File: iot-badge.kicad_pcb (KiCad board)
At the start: 2 copper layers, 70 x 100 mm, 30 parts, among them J1 USB_C_Receptacle_USB2.0, Q1 BC847, Q2 BC847, SW1 SW_Push, SW2 SW_Push, SW3 SW_Push, SW4 SW_Push, SW5 SW_Push, SW6 SW_Push, U1 ESP32-WROOM-32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

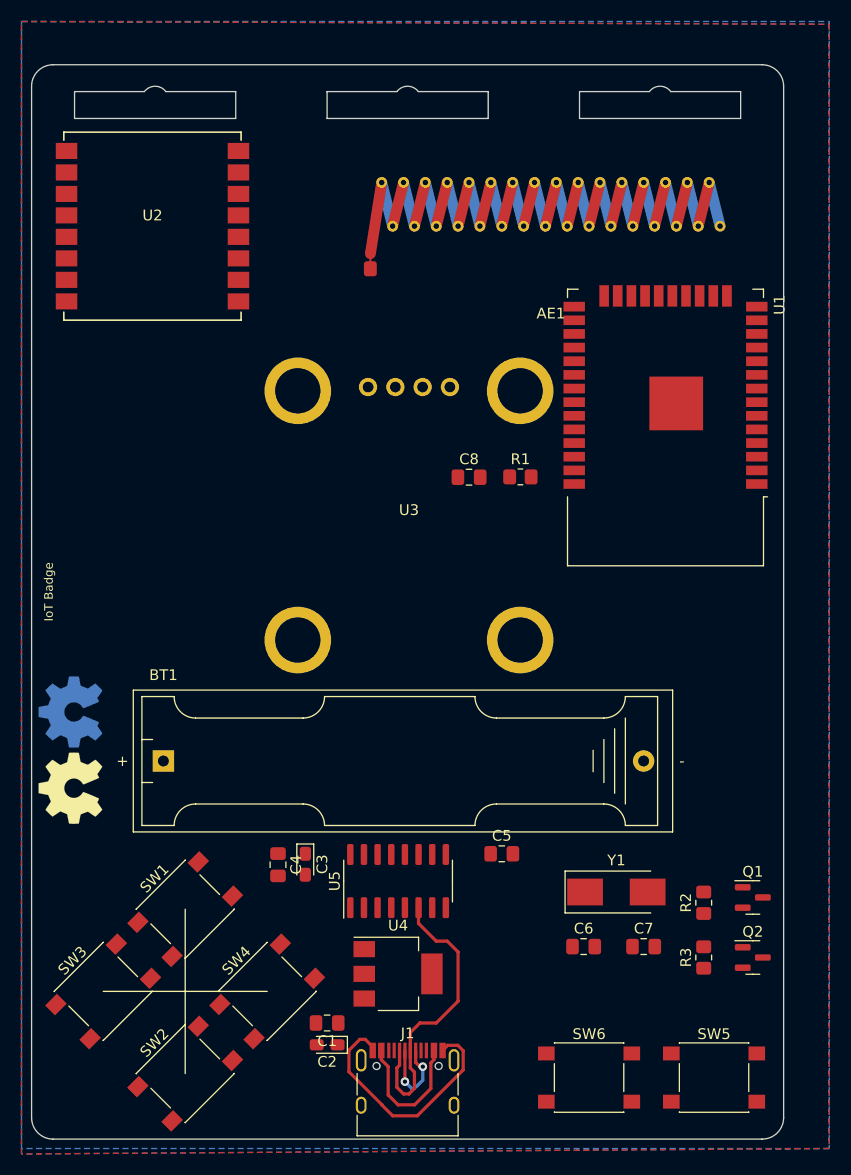
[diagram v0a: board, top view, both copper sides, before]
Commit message: pcb ant fixed
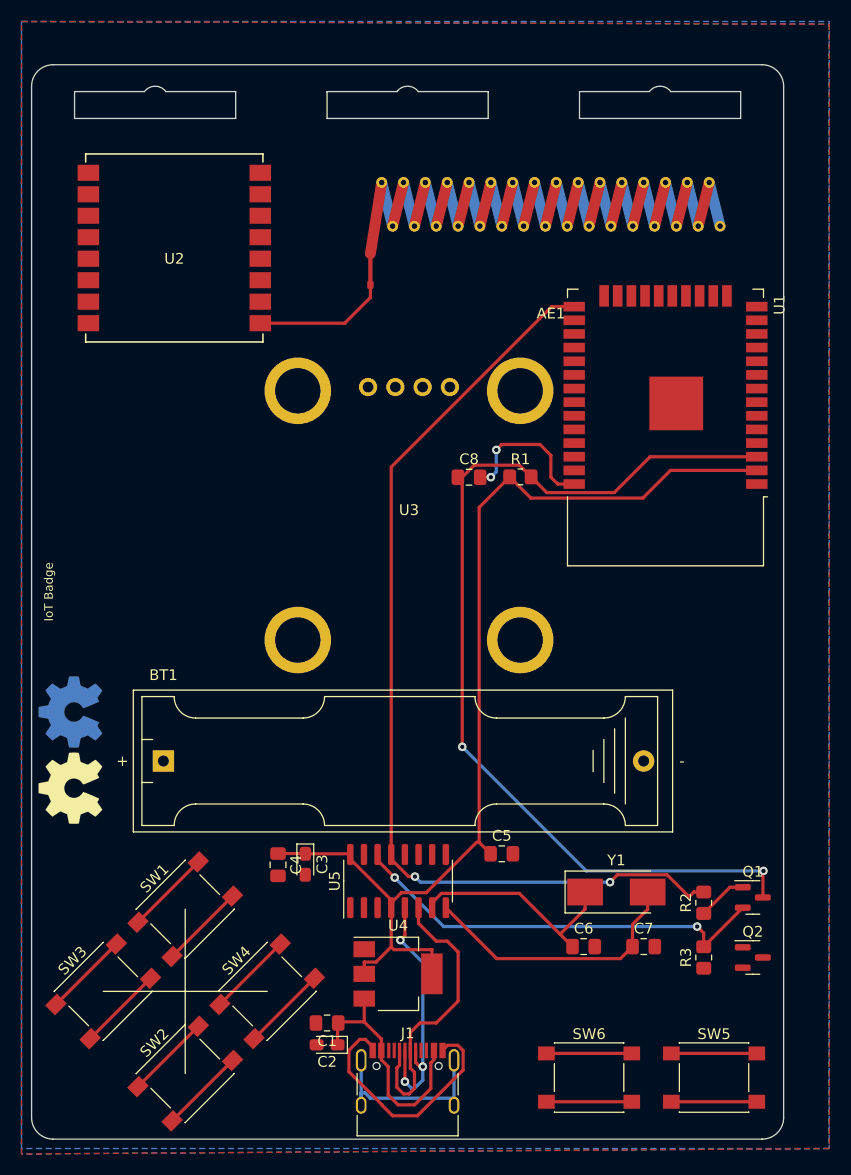
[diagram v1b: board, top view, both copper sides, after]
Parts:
- U2: value Ai-Thinker-Ra-02 -> Ai-Thinker-Ra-02-alt; footprint RF_Module:Ai-Thinker-Ra-01-LoRa -> RF_Module_alt:Ai-Thinker-Ra-02-LoRa-alt
- moved U2 2.87 mm to (113.3, 67.1), turned to 180 degrees
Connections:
- AE1 pad 1: Net-(AE1-Pad1) -> Net-(U2-Pad1)
- Q2 pad 2: /IO0 -> Net-(Q2-Pad2)
- Q2 pad 3: unconnected-(Q2-Pad3) -> /IO0
- R2 pad 2: /IO0 -> Net-(Q2-Pad2)
- U2 pad 1: unconnected-(U2-Pad1) -> Net-(U2-Pad1)
- U2 pad 14: Net-(AE1-Pad1) -> unconnected-(U2-Pad14)
- U2 pad 16: unconnected-(U2-Pad1) -> Earth
- U2 pad 2: unconnected-(U2-Pad1) -> Earth
- U2 pad 3: unconnected-(U2-Pad3) -> +3V3
- U2 pad 9: unconnected-(U2-Pad1) -> Earth
- U3 pad 1: unconnected-(U3-Pad1) -> Earth
- U3 pad 2: unconnected-(U3-Pad2) -> +3V3
- U5 pad 13: /IO0 -> Net-(Q2-Pad2)
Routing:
- net +3V3: track 0.00 -> 99.3 mm
- net /EN: track 0.00 -> 91.1 mm, vias 0 -> 2
- net Net-(Q2-Pad2): track 0.00 -> 91.0 mm, vias 0 -> 2
- net Net-(Q1-Pad2): track 0.00 -> 40.1 mm, vias 0 -> 2
- net Net-(C7-Pad1): track 0.00 -> 25.5 mm
- net Net-(C6-Pad1): track 0.00 -> 20.8 mm
- net unconnected-(J1-PadS1): track 0.00 -> 18.4 mm
- net Net-(J1-PadA6): track 8.34 -> 24.2 mm, vias 2 -> 3
- net Earth: track 23.5 -> 37.4 mm, vias 0 -> 2
- net Net-(U2-Pad1): track 0.00 -> 12.1 mm
- net Net-(C1-Pad1): track 13.1 -> 23.1 mm
- net unconnected-(SW3-Pad2): track 0.00 -> 7.95 mm
- net unconnected-(SW4-Pad2): track 0.00 -> 7.95 mm
- net unconnected-(SW4-Pad1): track 0.00 -> 7.95 mm
- net unconnected-(SW3-Pad1): track 0.00 -> 7.95 mm
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
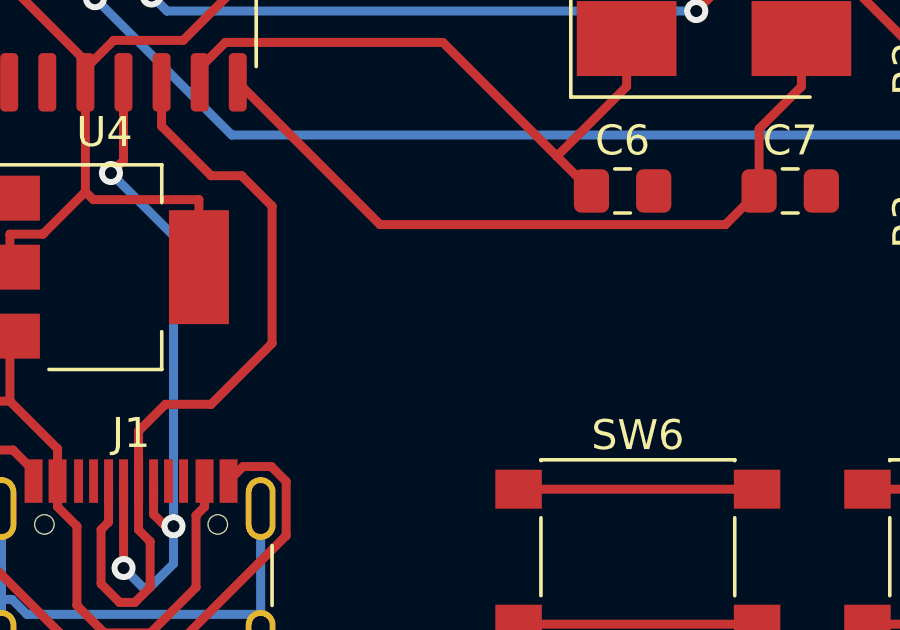
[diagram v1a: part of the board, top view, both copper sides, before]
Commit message: connected lora and screen
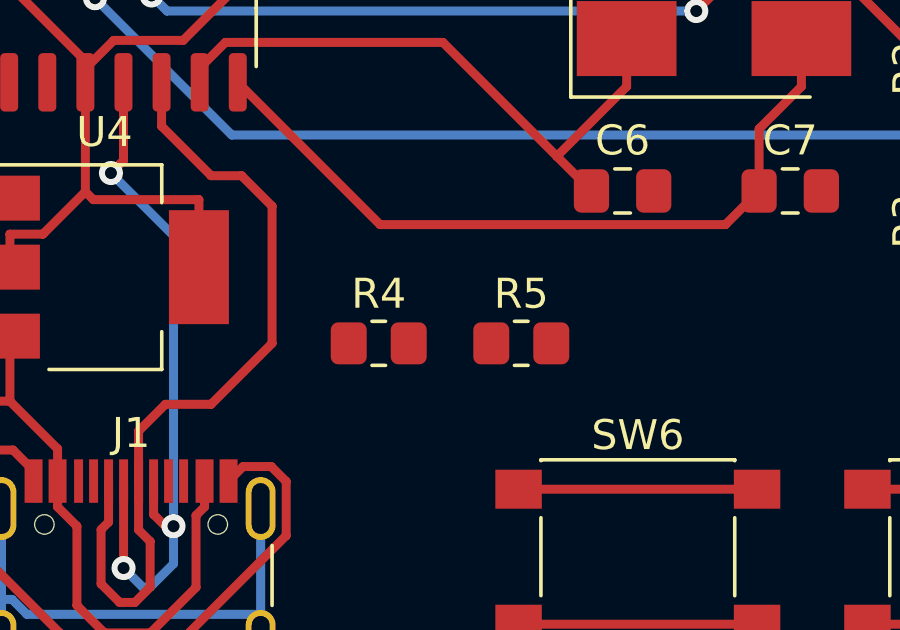
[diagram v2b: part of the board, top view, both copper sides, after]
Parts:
- added R4: 5.1k, Resistor_SMD:R_0805_2012Metric_Pad1.20x1.40mm_HandSolder, F.Cu at (143.3, 137.2)
- added R5: 5.1k, Resistor_SMD:R_0805_2012Metric_Pad1.20x1.40mm_HandSolder, F.Cu at (148.0, 137.2)
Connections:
- J1 pad A5: unconnected-(J1-PadA5) -> Net-(J1-PadA5)
- J1 pad B5: unconnected-(J1-PadB5) -> Net-(J1-PadB5)
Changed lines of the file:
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@@
   (net 47 "unconnected-(U1-Pad37)")
   (net 48 "Net-(Q1-Pad2)")
-  (net 49 "Net-(U2-Pad1)")
+  (net 49 "Net-(AE1-Pad1)")
   (net 50 "unconnected-(U2-Pad4)")
   (net 51 "unconnected-(U2-Pad5)")
@@
   (net 61 "unconnected-(BT1-Pad2)")
   (net 62 "Earth")
-  (net 63 "unconnected-(J1-PadA5)")
+  (net 63 "Net-(J1-PadA5)")
   (net 64 "unconnected-(J1-PadA8)")
-  (net 65 "unconnected-(J1-PadB5)")
+  (net 65 "Net-(J1-PadB5)")
   (net 66 "unconnected-(J1-PadB8)")
   (net 67 "unconnected-(J1-PadS1)")
@@
     (pad "" thru_hole circle (at 7.62 2.032) (size 1 1) (drill 0.508) (layers *.Cu))
     (pad "1" smd roundrect (at -16.8 7.5) (size 0.6 0.75) (layers "F.Cu") (roundrect_rratio 0.2083333333)
-      (net 49 "Net-(U2-Pad1)") (pinfunction "A") (pintype "input"))
+      (net 49 "Net-(AE1-Pad1)") (pinfunction "A") (pintype "input"))
     (zone (net 0) (net_name "") (layers "F.Cu" "F.CrtYd") (hatch full 0.508)
       (connect_pads (clearance 0))
@@
       (net 13 "Net-(C1-Pad1)") (pinfunction "VBUS") (pintype "passive"))
     (pad "A5" smd rect (at -1.25 -4.045) (size 0.3 1.45) (layers "F.Cu" "F.Paste" "F.Mask")
-      (net 63 "unconnected-(J1-PadA5)") (pinfunction "CC1") (pintype "bidirectional+no_connect"))
+      (net 63 "Net-(J1-PadA5)") (pinfunction "CC1") (pintype "bidirectional"))
     (pad "A6" smd rect (at -0.25 -4.045) (size 0.3 1.45) (layers "F.Cu" "F.Paste" "F.Mask")
       (net 81 "Net-(J1-PadA6)") (pinfunction "D+") (pintype "bidirectional"))
@@
       (net 13 "Net-(C1-Pad1)") (pinfunction "VBUS") (pintype "passive"))
     (pad "B5" smd rect (at 1.75 -4.045) (size 0.3 1.45) (layers "F.Cu" "F.Paste" "F.Mask")
-      (net 65 "unconnected-(J1-PadB5)") (pinfunction "CC2") (pintype "bidirectional+no_connect"))
+      (net 65 "Net-(J1-PadB5)") (pinfunction "CC2") (pintype "bidirectional"))
     (pad "B6" smd rect (at 0.75 -4.045) (size 0.3 1.45) (layers "F.Cu" "F.Paste" "F.Mask")
       (net 81 "Net-(J1-PadA6)") (pinfunction "D+") (pintype "bidirectional"))
@@
       (net 62 "Earth") (pintype "passive"))
     (model "${KICAD6_3DMODEL_DIR}/Capacitor_SMD.3dshapes/C_0805_2012Metric.wrl"
+      (offset (xyz 0 0 0))
+      (scale (xyz 1 1 1))
+      (rotate (xyz 0 0 0))
+    )
+  )
+  (footprint "Resistor_SMD:R_0805_2012Metric_Pad1.20x1.40mm_HandSolder" (layer "F.Cu")
+    (at 143.256 137.16)
+    (descr "Resistor SMD 0805 (2012 Metric), square (rectangular) end terminal, IPC_7351 nominal with elongated pad for handsoldering. (Body size source: IPC-SM-782 page 72, https://www.pcb-3d.com/wordpress/wp-content/uploads/ipc-sm-782a_amendment_1_and_2.pdf), generated with kicad-footprint-generator")
+    (tags "resistor handsolder")
+    (property "Sheetfile" "iot-badge.kicad_sch")
+    (property "Sheetname" "")
+    (attr smd)
+    (fp_text reference "R4" (at 0 -1.65) (layer "F.SilkS")
+      (effects (font (size 1 1) (thickness 0.15)))
+    )
+    (fp_text value "5.1k" (at 0 1.65) (layer "F.Fab")
+      (effects (font (size 1 1) (thickness 0.15)))
+    )
+    (fp_text user "${REFERENCE}" (at 0 0) (layer "F.Fab")
+      (effects (font (size 0.5 0.5) (thickness 0.08)))
+    )
+    (fp_line (start -0.227064 0.735) (end 0.227064 0.735) (layer "F.SilkS") (width 0.12))
+    (fp_line (start -0.227064 -0.735) (end 0.227064 -0.735) (layer "F.SilkS") (width 0.12))
+    (fp_line (start -1.85 -0.95) (end 1.85 -0.95) (layer "F.CrtYd") (width 0.05))
+    (fp_line (start 1.85 -0.95) (end 1.85 0.95) (layer "F.CrtYd") (width 0.05))
+    (fp_line (start 1.85 0.95) (end -1.85 0.95) (layer "F.CrtYd") (width 0.05))
+    (fp_line (start -1.85 0.95) (end -1.85 -0.95) (layer "F.CrtYd") (width 0.05))
+    (fp_line (start 1 -0.625) (end 1 0.625) (layer "F.Fab") (width 0.1))
+    (fp_line (start 1 0.625) (end -1 0.625) (layer "F.Fab") (width 0.1))
+    (fp_line (start -1 -0.625) (end 1 -0.625) (layer "F.Fab") (width 0.1))
+    (fp_line (start -1 0.625) (end -1 -0.625) (layer "F.Fab") (width 0.1))
+    (pad "1" smd roundrect (at -1 0) (size 1.2 1.4) (layers "F.Cu" "F.Paste" "F.Mask") (roundrect_rratio 0.208333)
+      (net 65 "Net-(J1-PadB5)") (pintype "passive"))
+    (pad "2" smd roundrect (at 1 0) (size 1.2 1.4) (layers "F.Cu" "F.Paste" "F.Mask") (roundrect_rratio 0.208333)
+      (net 62 "Earth") (pintype "passive"))
+    (model "${KICAD6_3DMODEL_DIR}/Resistor_SMD.3dshapes/R_0805_2012Metric.wrl"
       (offset (xyz 0 0 0))
       (scale (xyz 1 1 1))
@@
     )
   )
+  (footprint "Resistor_SMD:R_0805_2012Metric_Pad1.20x1.40mm_HandSolder" (layer "F.Cu")
+    (at 148.006 137.16)
+    (descr "Resistor SMD 0805 (2012 Metric), square (rectangular) end terminal, IPC_7351 nominal with elongated pad for handsoldering. (Body size source: IPC-SM-782 page 72, https://www.pcb-3d.com/wordpress/wp-content/uploads/ipc-sm-782a_amendment_1_and_2.pdf), generated with kicad-footprint-generator")
+    (tags "resistor handsolder")
+    (property "Sheetfile" "iot-badge.kicad_sch")
+    (property "Sheetname" "")
+    (attr smd)
+    (fp_text reference "R5" (at 0 -1.65) (layer "F.SilkS")
+      (effects (font (size 1 1) (thickness 0.15)))
+    )
+    (fp_text value "5.1k" (at 0 1.65) (layer "F.Fab")
+      (effects (font (size 1 1) (thickness 0.15)))
+    )
+    (fp_text user "${REFERENCE}" (at 0 0) (layer "F.Fab")
+      (effects (font (size 0.5 0.5) (thickness 0.08)))
+    )
+    (fp_line (start -0.227064 0.735) (end 0.227064 0.735) (layer "F.SilkS") (width 0.12))
+    (fp_line (start -0.227064 -0.735) (end 0.227064 -0.735) (layer "F.SilkS") (width 0.12))
+    (fp_line (start 1.85 0.95) (end -1.85 0.95) (layer "F.CrtYd") (width 0.05))
+    (fp_line (start -1.85 -0.95) (end 1.85 -0.95) (layer "F.CrtYd") (width 0.05))
+    (fp_line (start -1.85 0.95) (end -1.85 -0.95) (layer "F.CrtYd") (width 0.05))
+    (fp_line (start 1.85 -0.95) (end 1.85 0.95) (layer "F.CrtYd") (width 0.05))
+    (fp_line (start 1 0.625) (end -1 0.625) (layer "F.Fab") (width 0.1))
+    (fp_line (start -1 0.625) (end -1 -0.625) (layer "F.Fab") (width 0.1))
+    (fp_line (start 1 -0.625) (end 1 0.625) (layer "F.Fab") (width 0.1))
+    (fp_line (start -1 -0.625) (end 1 -0.625) (layer "F.Fab") (width 0.1))
+    (pad "1" smd roundrect (at -1 0) (size 1.2 1.4) (layers "F.Cu" "F.Paste" "F.Mask") (roundrect_rratio 0.208333)
+      (net 63 "Net-(J1-PadA5)") (pintype "passive"))
+    (pad "2" smd roundrect (at 1 0) (size 1.2 1.4) (layers "F.Cu" "F.Paste" "F.Mask") (roundrect_rratio 0.208333)
+      (net 62 "Earth") (pintype "passive"))
+    (model "${KICAD6_3DMODEL_DIR}/Resistor_SMD.3dshapes/R_0805_2012Metric.wrl"
+      (offset (xyz 0 0 0))
+      (scale (xyz 1 1 1))
+      (rotate (xyz 0 0 0))
+    )
+  )
   (footprint "Package_TO_SOT_SMD:SOT-23" (layer "F.Cu")
     (at 167.132 133.096)
@@
     (fp_line (start -8 8.5) (end -8 -8.5) (layer "F.Fab") (width 0.15))
     (pad "1" smd rect (at -8 -7 180) (size 2 1.5) (layers "F.Cu" "F.Paste" "F.Mask")
-      (net 49 "Net-(U2-Pad1)") (pinfunction "ANT") (pintype "bidirectional"))
+      (net 49 "Net-(AE1-Pad1)") (pinfunction "ANT") (pintype "bidirectional"))
     (pad "2" smd rect (at -8 -5 180) (size 2 1.5) (layers "F.Cu" "F.Paste" "F.Mask")
       (net 62 "Earth") (pinfunction "GND") (pintype "power_in"))

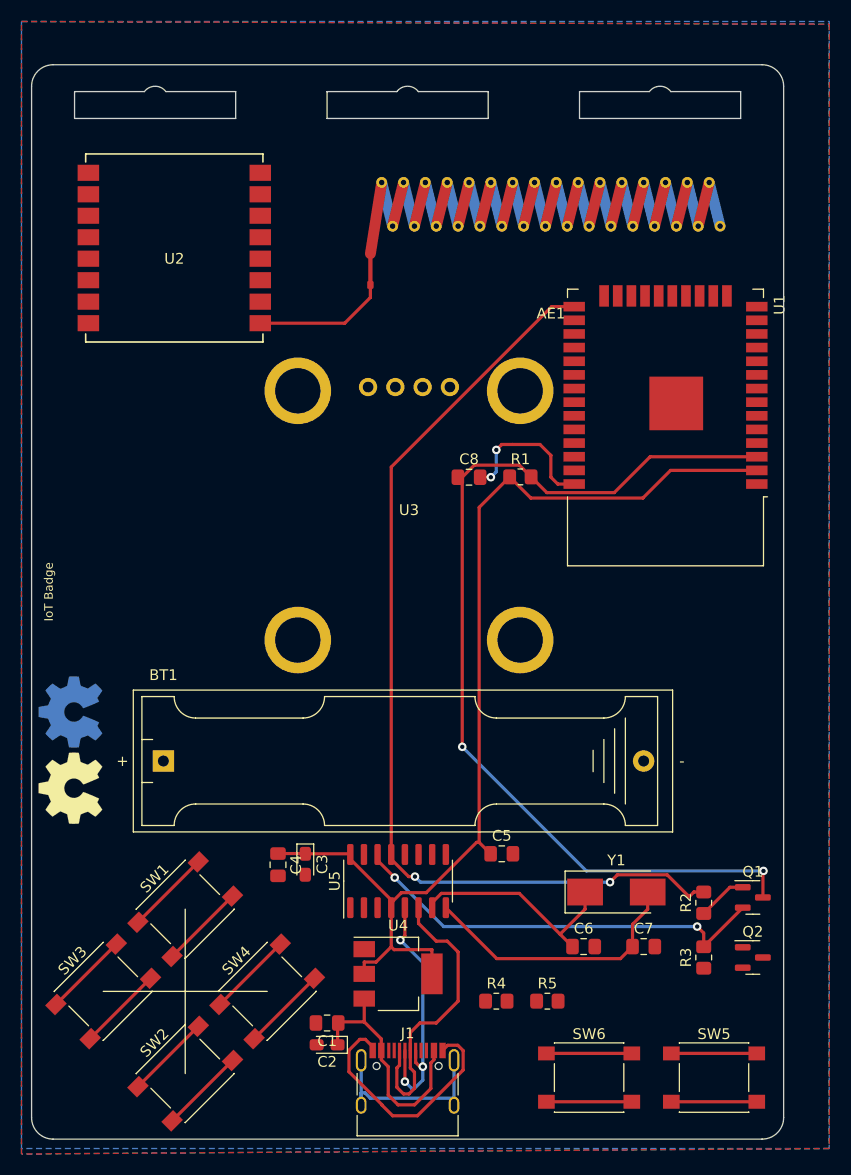
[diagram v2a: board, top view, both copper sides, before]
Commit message: added res buttons and almost routable
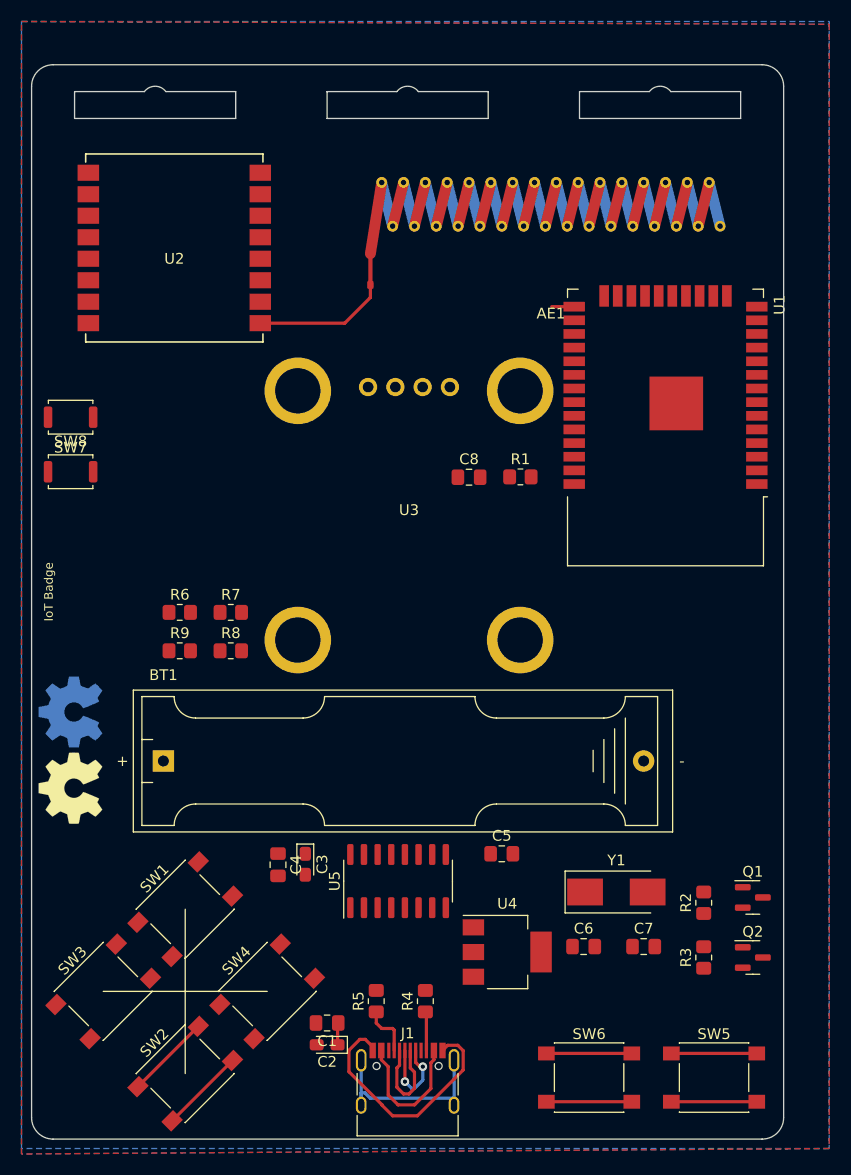
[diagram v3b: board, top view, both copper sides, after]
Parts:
- added R6: 10k, Resistor_SMD:R_0805_2012Metric_Pad1.20x1.40mm_HandSolder, F.Cu at (113.8, 101.0)
- added R7: 10k, Resistor_SMD:R_0805_2012Metric_Pad1.20x1.40mm_HandSolder, F.Cu at (118.5, 101.0)
- added R8: 0, Resistor_SMD:R_0805_2012Metric_Pad1.20x1.40mm_HandSolder, F.Cu at (118.5, 104.5)
- added R9: 0, Resistor_SMD:R_0805_2012Metric_Pad1.20x1.40mm_HandSolder, F.Cu at (113.8, 104.5)
- added SW7: E, Button_Switch_SMD:SW_Push_SPST_NO_Alps_SKRK, F.Cu at (103.6, 87.9)
- added SW8: 0, Button_Switch_SMD:SW_Push_SPST_NO_Alps_SKRK, F.Cu at (103.6, 82.8)
- moved R5 15.9 mm to (132.1, 137.2), turned to 90 degrees
- moved U4 10.4 mm to (144.3, 132.6)
- moved R4 6.60 mm to (136.7, 137.2), turned to 90 degrees
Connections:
- U1 pad 11: unconnected-(U1-Pad11) -> Net-(U1-Pad11)
- U1 pad 12: unconnected-(U1-Pad12) -> Net-(U1-Pad12)
- U1 pad 13: unconnected-(U1-Pad13) -> Net-(U1-Pad13)
- U1 pad 23: unconnected-(U1-Pad23) -> Net-(U1-Pad23)
- U1 pad 26: unconnected-(U1-Pad26) -> Net-(U1-Pad26)
- U1 pad 29: unconnected-(U1-Pad29) -> Net-(U1-Pad29)
- U1 pad 30: unconnected-(U1-Pad30) -> Net-(U1-Pad30)
- U1 pad 31: unconnected-(U1-Pad31) -> Net-(U1-Pad31)
- U1 pad 34: unconnected-(U1-Pad34) -> Net-(U1-Pad34)
- U1 pad 35: unconnected-(U1-Pad35) -> Net-(U1-Pad35)
- U1 pad 6: unconnected-(U1-Pad6) -> Net-(U1-Pad6)
- U1 pad 7: unconnected-(U1-Pad7) -> Net-(U1-Pad7)
- U2 pad 12: unconnected-(U2-Pad12) -> Net-(U1-Pad29)
- U2 pad 13: unconnected-(U2-Pad13) -> Net-(U1-Pad31)
- U2 pad 14: unconnected-(U2-Pad14) -> Net-(U1-Pad12)
- U2 pad 15: unconnected-(U2-Pad15) -> Net-(U1-Pad30)
- U2 pad 4: unconnected-(U2-Pad4) -> Net-(U1-Pad13)
- U2 pad 5: unconnected-(U2-Pad5) -> Net-(U1-Pad11)
- U2 pad 6: unconnected-(U2-Pad6) -> Net-(U1-Pad7)
- U2 pad 7: unconnected-(U2-Pad7) -> Net-(U1-Pad6)
- U3 pad 3: unconnected-(U3-Pad3) -> Net-(U1-Pad23)
- U3 pad 4: unconnected-(U3-Pad4) -> Net-(U1-Pad26)
- U5 pad 2: unconnected-(U5-Pad2) -> Net-(U5-Pad2)
- U5 pad 3: unconnected-(U5-Pad3) -> Net-(U5-Pad3)
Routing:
- net +3V3: track 99.3 -> 0.00 mm
- net /EN: track 91.1 -> 0.00 mm, vias 2 -> 0
- net Net-(Q2-Pad2): track 91.0 -> 0.00 mm, vias 2 -> 0
- net Net-(Q1-Pad2): track 40.1 -> 0.00 mm, vias 2 -> 0
- net Net-(C7-Pad1): track 25.5 -> 0.00 mm
- net Net-(C6-Pad1): track 20.8 -> 0.00 mm
- net Net-(J1-PadA7): track 27.5 -> 9.33 mm
- net Net-(J1-PadA6): track 24.2 -> 8.34 mm, vias 3 -> 2
- net Earth: track 37.4 -> 23.5 mm, vias 2 -> 0
- net unconnected-(SW3-Pad2): track 7.95 -> 0.00 mm
- net unconnected-(SW4-Pad2): track 7.95 -> 0.00 mm
- net unconnected-(SW4-Pad1): track 7.95 -> 0.00 mm
- net unconnected-(SW3-Pad1): track 7.95 -> 0.00 mm
- net unconnected-(SW1-Pad2): track 7.95 -> 0.00 mm
- net unconnected-(SW1-Pad1): track 7.95 -> 0.00 mm
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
